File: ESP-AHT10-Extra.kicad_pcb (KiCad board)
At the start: 2 copper layers, 38.2 x 20.8 mm, 23 parts, among them J1 USB, SW1 RESET, SW2 PROG, U1 CH330N, U2 HT7233, U3 ESP-12, U4 AHT10, U5 USBLC6-2SC6

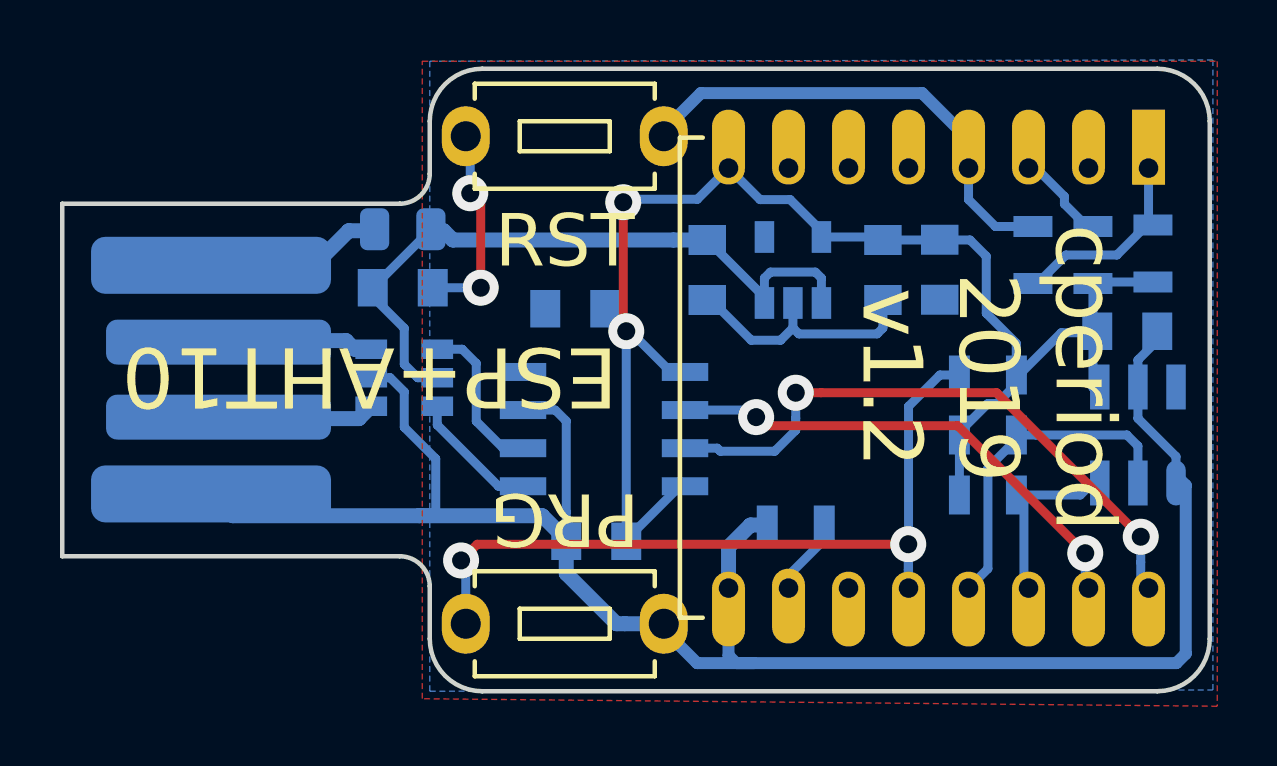
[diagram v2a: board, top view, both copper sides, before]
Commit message: switch CH300N to 5V, add 330R resistors to TX/RD, tweak GPIO0 connection, adjust ground connections
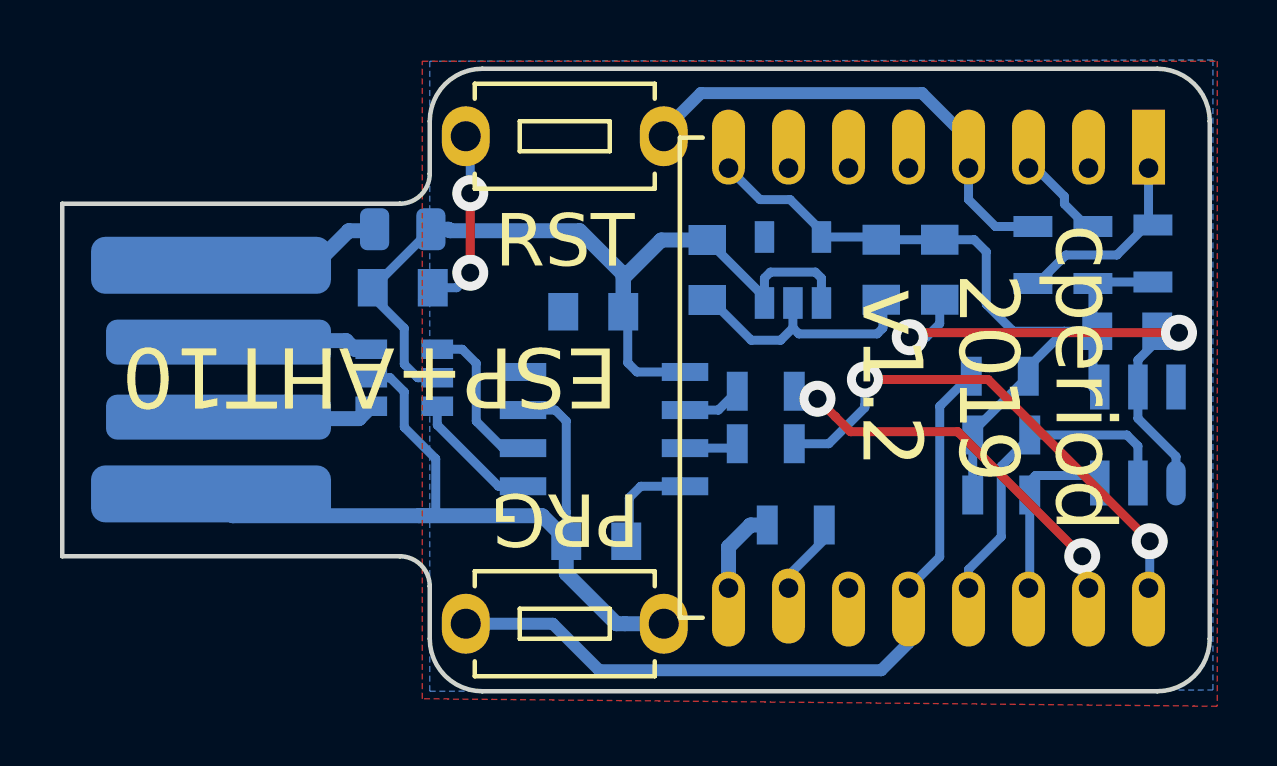
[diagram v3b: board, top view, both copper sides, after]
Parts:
- added R8: 330R, Resistors_SMD:R_0805, B.Cu at (153.4, 99.5)
- added R9: 330R, Resistors_SMD:R_0805, B.Cu at (153.4, 97.8)
- moved C1 10.3 mm to (157.3, 93.7), turned to 270 degrees
- moved C3 9.76 mm to (147.7, 95.1), turned to 0 degrees
- moved R6 0.44 mm to (161.3, 99.2)
- moved R7 0.44 mm to (161.3, 101.2)
- moved R5 0.40 mm to (161.2, 97.2)
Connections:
- C3 pad 2: 3V3 -> 5V
- C6 pad 1: 3V3 -> Net-(C6-Pad1)
- U1 pad 5: 3V3 -> 5V
- U1 pad 6: eRX -> Net-(R9-Pad2)
- U1 pad 7: eTX -> Net-(R8-Pad2)
- U1 pad 8: 3V3 -> Net-(C6-Pad1)
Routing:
- net 3V3: track 49.7 -> 28.2 mm, vias 2 -> 0
- net GND: track 81.1 -> 64.7 mm, vias 2 -> 4
- net 5V: track 23.0 -> 29.8 mm
- net Net-(C6-Pad1): track 0.00 -> 3.49 mm
- net eRX: track 16.5 -> 13.0 mm
- net eTX: track 20.6 -> 17.1 mm
- net Net-(R9-Pad2): track 0.00 -> 2.00 mm
- net Net-(R8-Pad2): track 0.00 -> 1.80 mm
- net Net-(R5-Pad2): track 27.0 -> 25.5 mm, vias 2 -> 0
- net SCL: track 6.32 -> 5.54 mm

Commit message: more direct 5V routing
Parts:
- turned C2 to 90 degrees
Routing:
- net 5V: track 29.8 -> 27.9 mm
- net GND: track 64.7 -> 65.3 mm
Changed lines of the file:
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@@
     (thickness 1.6)
     (drawings 18)
-    (tracks 193)
+    (tracks 195)
     (zones 0)
     (modules 25)
@@
   )
   (setup
-    (last_trace_width 0.4)
+    (last_trace_width 0.3)
     (user_trace_width 0.4)
     (user_trace_width 0.5)
@@
   )
   (module Capacitors_SMD:C_0805 (layer B.Cu)
-    (at 151.5 93.70862 270)
+    (at 151.5 93.70862 90)
     (descr "Capacitor SMD 0805, reflow soldering, AVX (see smccp.pdf)")
     (tags "capacitor 0805")
     (attr smd)
-    (fp_text reference C2 (at -2.30862 -0.044297 180) (layer B.SilkS)
-      (effects (font (size 1 1) (thickness 0.15)) (justify mirror))
-    )
-    (fp_text value 10u (at -8.45862 -0.25 270) (layer B.Fab)
+    (fp_text reference C2 (at -2.30862 -0.044297) (layer B.SilkS)
+      (effects (font (size 1 1) (thickness 0.15)) (justify mirror))
+    )
+    (fp_text value 10u (at -8.45862 -0.25 90) (layer B.Fab)
       (effects (font (size 1 1) (thickness 0.15)) (justify mirror))
     )
@@
     (fp_line (start 1 -0.62) (end -1 -0.62) (layer B.Fab) (width 0.1))
     (fp_line (start -1 -0.62) (end -1 0.62) (layer B.Fab) (width 0.1))
-    (fp_text user %R (at 0 1.5 270) (layer B.Fab) hide
-      (effects (font (size 1 1) (thickness 0.15)) (justify mirror))
-    )
-    (pad 2 smd rect (at 1 0 270) (size 1 1.25) (layers B.Cu B.Paste B.Mask)
-      (net 2 GND))
-    (pad 1 smd rect (at -1 0 270) (size 1 1.25) (layers B.Cu B.Paste B.Mask)
+    (fp_text user %R (at 0 1.5 90) (layer B.Fab) hide
+      (effects (font (size 1 1) (thickness 0.15)) (justify mirror))
+    )
+    (pad 2 smd rect (at 1 0 90) (size 1 1.25) (layers B.Cu B.Paste B.Mask)
+      (net 2 GND))
+    (pad 1 smd rect (at -1 0 90) (size 1 1.25) (layers B.Cu B.Paste B.Mask)
       (net 18 5V))
     (model Capacitors_SMD.3dshapes/C_0805.wrl
@@
   (segment (start 146.8 103.825) (end 148.475 105.5) (width 0.5) (layer B.Cu) (net 2))
   (segment (start 146.8 102.7) (end 146.8 103.825) (width 0.5) (layer B.Cu) (net 2))
-  (segment (start 151.625 94.70862) (end 151.5 94.70862) (width 0.3) (layer B.Cu) (net 2))
-  (segment (start 152.966367 96.049987) (end 151.625 94.70862) (width 0.3) (layer B.Cu) (net 2))
+  (segment (start 151.625 94.70862) (end 151.5 94.70862) (width 0.3) (layer B.Cu) (net 18))
   (segment (start 154.355703 95.63862) (end 153.944336 96.049987) (width 0.3) (layer B.Cu) (net 2))
   (segment (start 153.944336 96.049987) (end 152.966367 96.049987) (width 0.3) (layer B.Cu) (net 2))
@@
   (segment (start 158.25 95.95) (end 158.8 95.95) (width 0.3) (layer B.Cu) (net 2))
   (segment (start 158.8 95.95) (end 159.25 95.5) (width 0.3) (layer B.Cu) (net 2))
+  (segment (start 151.021591 105.5) (end 152.209217 104.312374) (width 0.4) (layer B.Cu) (net 2))
+  (segment (start 150.05 105.5) (end 151.021591 105.5) (width 0.4) (layer B.Cu) (net 2))
   (segment (start 159.25 98.25) (end 160.25 97.25) (width 0.3) (layer B.Cu) (net 9))
   (segment (start 158.209217 104.312374) (end 159.25 103.271591) (width 0.3) (layer B.Cu) (net 9))
@@
   (segment (start 149.282626 100.917374) (end 148.9 101.3) (width 0.3) (layer B.Cu) (net 17))
   (segment (start 153.405703 94.614323) (end 153.405703 94.80862) (width 0.3) (layer B.Cu) (net 18))
-  (segment (start 151.5 92.70862) (end 153.405703 94.614323) (width 0.3) (layer B.Cu) (net 18))
-  (segment (start 155.105702 93.778619) (end 155.305703 93.97862) (width 0.3) (layer B.Cu) (net 18))
-  (segment (start 153.605704 93.778619) (end 155.105702 93.778619) (width 0.3) (layer B.Cu) (net 18))
-  (segment (start 155.305703 93.97862) (end 155.305703 94.80862) (width 0.3) (layer B.Cu) (net 18))
-  (segment (start 153.405703 93.97862) (end 153.605704 93.778619) (width 0.3) (layer B.Cu) (net 18))
-  (segment (start 153.405703 94.80862) (end 153.405703 93.97862) (width 0.3) (layer B.Cu) (net 18))
   (segment (start 142.125 92.525) (end 142.125 92.4) (width 0.3) (layer B.Cu) (net 18))
   (segment (start 140.35 94.3) (end 142.125 92.525) (width 0.3) (layer B.Cu) (net 18))
@@
   (segment (start 148.7 93.85) (end 148.7 95.1) (width 0.5) (layer B.Cu) (net 18))
   (segment (start 147.25 92.4) (end 148.7 93.85) (width 0.5) (layer B.Cu) (net 18))
-  (segment (start 149.96638 92.70862) (end 151.5 92.70862) (width 0.5) (layer B.Cu) (net 18))
-  (segment (start 148.7 95.1) (end 148.7 93.975) (width 0.5) (layer B.Cu) (net 18))
-  (segment (start 148.7 93.975) (end 149.96638 92.70862) (width 0.5) (layer B.Cu) (net 18))
+  (segment (start 149.05 94.75) (end 151.5 94.75) (width 0.5) (layer B.Cu) (net 18))
+  (segment (start 148.7 95.1) (end 149.05 94.75) (width 0.5) (layer B.Cu) (net 18))
+  (segment (start 153.305703 94.70862) (end 153.405703 94.80862) (width 0.3) (layer B.Cu) (net 18))
+  (segment (start 151.5 94.70862) (end 153.305703 94.70862) (width 0.3) (layer B.Cu) (net 18))
+  (segment (start 153.55 93.7) (end 155.15 93.7) (width 0.3) (layer B.Cu) (net 18))
+  (segment (start 155.15 93.7) (end 155.305703 93.855703) (width 0.3) (layer B.Cu) (net 18))
+  (segment (start 153.4 93.85) (end 153.55 93.7) (width 0.3) (layer B.Cu) (net 18))
+  (segment (start 155.305703 93.855703) (end 155.305703 94.80862) (width 0.3) (layer B.Cu) (net 18))
+  (segment (start 153.405703 94.80862) (end 153.405703 93.855703) (width 0.3) (layer B.Cu) (net 18))
+  (segment (start 153.405703 93.855703) (end 153.4 93.85) (width 0.3) (layer B.Cu) (net 18))
   (segment (start 152.352626 99.647374) (end 152.5 99.5) (width 0.3) (layer B.Cu) (net 19))
   (segment (start 150.759217 99.647374) (end 152.352626 99.647374) (width 0.3) (layer B.Cu) (net 19))

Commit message: more fine tuning, layout cleanup, stability fixes
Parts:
- removed R9: 330R, Resistors_SMD:R_0805
- added C8: 10u, Capacitors_SMD:C_0805, B.Cu at (151.5, 93.7)
- added D1: B5817W, Diodes_SMD:D_SOD-123F, B.Cu at (140.6, 93.8)
- moved C7 4.29 mm to (145.6, 93.8), turned to 90 degrees
- moved F1 2.52 mm to (143.5, 93.7), turned to 90 degrees
- moved C2 1.98 mm to (149.5, 93.8)
- moved U5 1.43 mm to (141.3, 98.7)
- moved C3 1.36 mm to (147.6, 93.8), turned to 90 degrees
- moved R8 0.90 mm to (152.9, 98.8), turned to 270 degrees
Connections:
- C3 pad 1: GND -> 5V
- C3 pad 2: 5V -> GND
- F1 pad 2: VBUS -> Net-(D1-Pad1)
- U1 pad 6: Net-(R9-Pad2) -> eRX
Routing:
- net GND: track 65.3 -> 71.8 mm
- net eRX: track 13.0 -> 17.0 mm
- net Net-(D1-Pad1): track 0.00 -> 3.88 mm
- net 5V: track 27.9 -> 24.4 mm
- net Net-(R9-Pad2): track 2.00 -> 0.00 mm
- net UDP-: track 5.36 -> 4.46 mm
- net VBUS: track 5.77 -> 6.35 mm
- net UDP+: track 4.34 -> 3.80 mm
- net UD-: track 5.21 -> 5.73 mm
